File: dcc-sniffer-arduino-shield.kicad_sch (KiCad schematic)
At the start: 9 parts, among them J1 MV132, U1 6N137

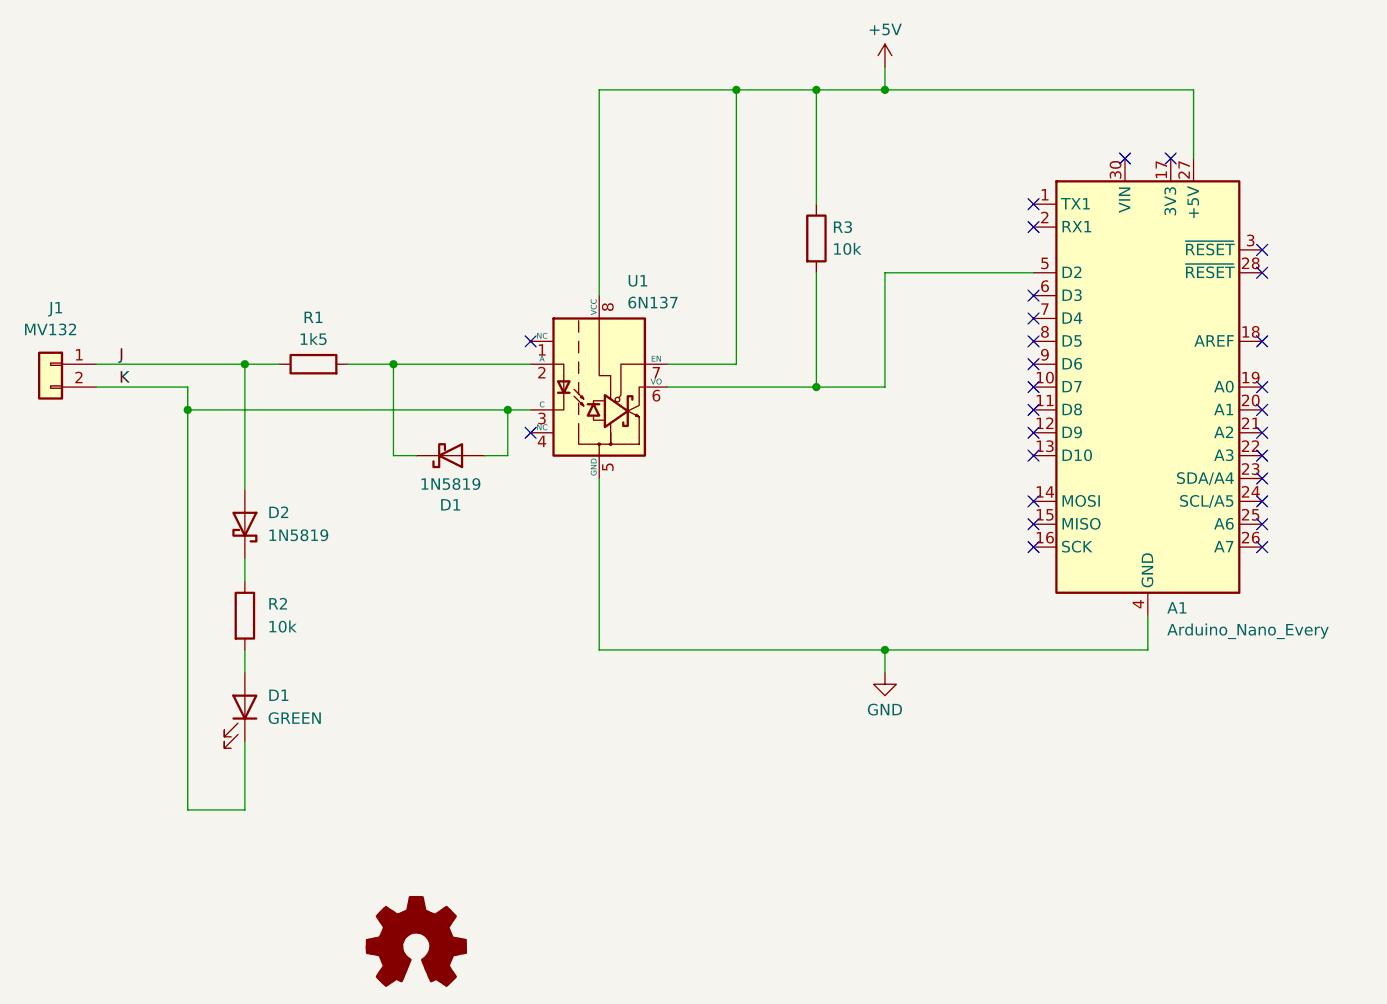
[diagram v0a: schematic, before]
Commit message: Route PCB.
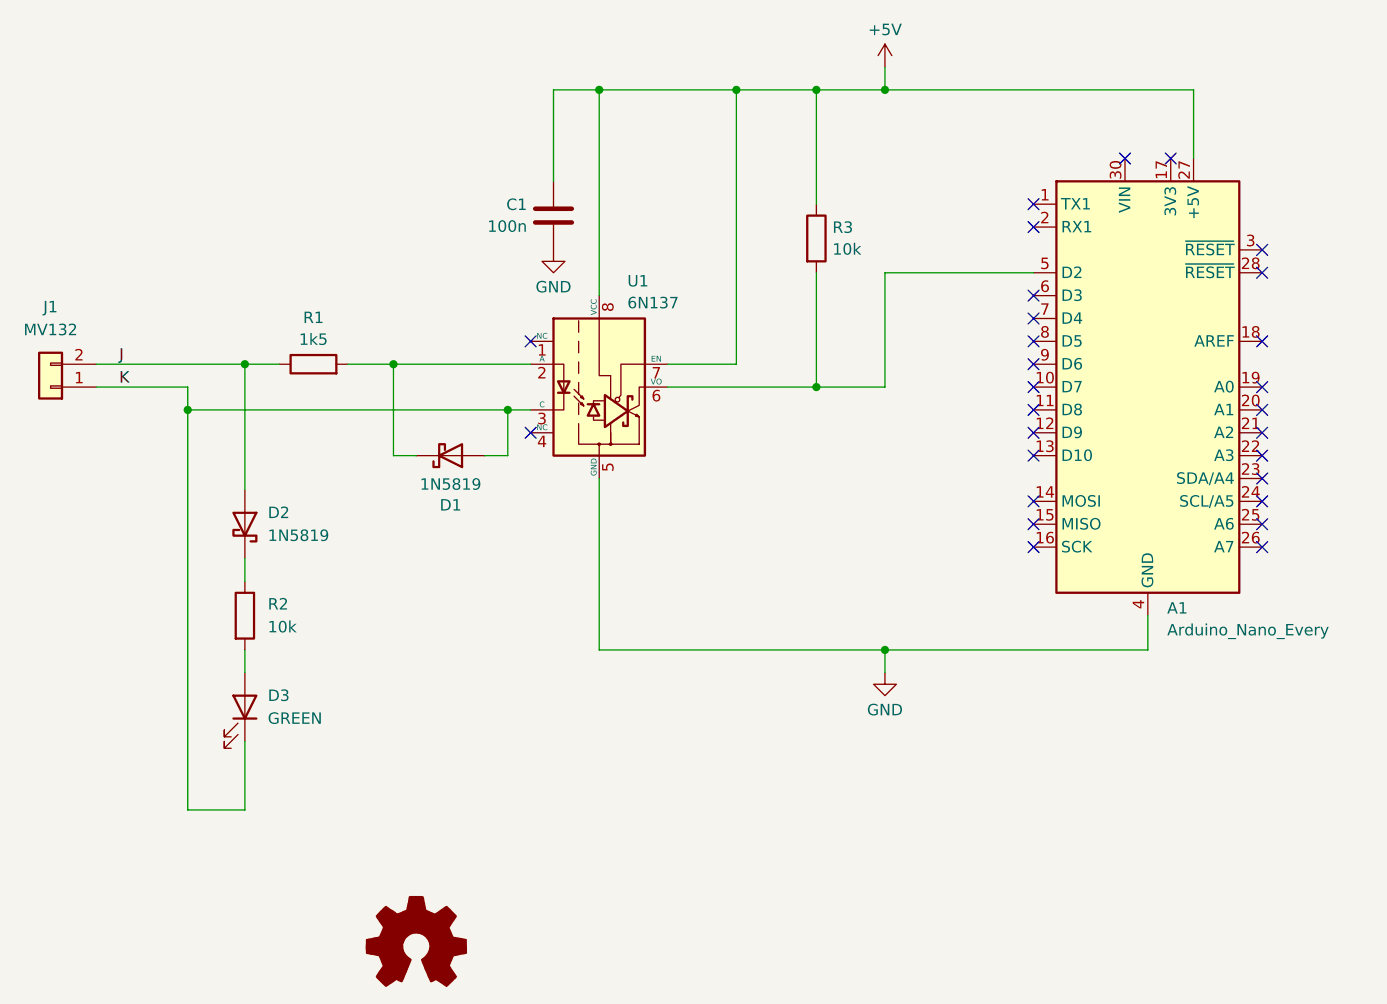
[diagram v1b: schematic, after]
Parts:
- added C1: 100n, Capacitor_SMD:C_0805_2012Metric_Pad1.18x1.45mm_HandSolder, symbol Device:C
- renumbered D1 to D3
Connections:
- net +5V: now also C1.1
- net GND: now also C1.2
- net J: now also J1.2 (Pin_2); no longer J1.1 (Pin_1)
- net K: now also J1.1 (Pin_1); no longer J1.2 (Pin_2)
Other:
- moved on the sheet: J1
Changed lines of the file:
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@@
+	)
+	(junction
+		(at 93.98 24.13)
+		(diameter 0)
+		(color 0 0 0 0)
 	)
 	(junction
@@
 	(wire
 		(pts
+			(xy 88.9 24.13) (xy 88.9 34.29)
+		)
+		(stroke
+			(width 0)
+			(type default)
+		)
+	)
+	(wire
+		(pts
 			(xy 48.26 104.14) (xy 48.26 59.69)
 		)
@@
 		(pts
 			(xy 54.61 54.61) (xy 54.61 68.58)
+		)
+		(stroke
+			(width 0)
+			(type default)
+		)
+	)
+	(wire
+		(pts
+			(xy 93.98 24.13) (xy 88.9 24.13)
 		)
 		(stroke
@@
 		(on_board yes)
 		(dnp no)
-		(property "Reference" "D1"
+		(property "Reference" "D3"
 			(at 57.15 91.44 90)
 			(effects
@@
 			(project ""
 				(path "/4adb1040-e115-4483-a004-02188402dddd"
-					(reference "D1")
+					(reference "D3")
 					(unit 1)
 				)
@@
 		(at 73.66 119.38 0)
 		(unit 1)
-		(exclude_from_sim no)
+		(exclude_from_sim yes)
 		(in_bom no)
 		(on_board no)
@@
 		)
 		(property "Description" "Open Hardware logo, small"
-			(at 73.66 119.38 0)
-			(effects
-				(font
-					(size 1.27 1.27)
-				)
-				(hide yes)
-			)
-		)
-		(property "Sim.Enable" "0"
 			(at 73.66 119.38 0)
 			(effects
@@
 	(symbol
 		(lib_id "power:GND")
+		(at 88.9 41.91 0)
+		(mirror y)
+		(unit 1)
+		(exclude_from_sim no)
+		(in_bom yes)
+		(on_board yes)
+		(dnp no)
+		(property "Reference" "#PWR03"
+			(at 88.9 48.26 0)
+			(effects
+				(font
+					(size 1.27 1.27)
+				)
+				(hide yes)
+			)
+		)
+		(property "Value" "GND"
+			(at 88.9 46.0431 0)
+			(effects
+				(font
+					(size 1.27 1.27)
+				)
+			)
+		)
+		(property "Footprint" ""
+			(at 88.9 41.91 0)
+			(effects
+				(font
+					(size 1.27 1.27)
+				)
+				(hide yes)
+			)
+		)
+		(property "Datasheet" ""
+			(at 88.9 41.91 0)
+			(effects
+				(font
+					(size 1.27 1.27)
+				)
+				(hide yes)
+			)
+		)
+		(property "Description" "Power symbol creates a global label with name \"GND\" , ground"
+			(at 88.9 41.91 0)
+			(effects
+				(font
+					(size 1.27 1.27)
+				)
+				(hide yes)
+			)
+		)
+		(pin "1"
+		)
+		(instances
+			(project "dcc-sniffer-arduino-shield"
+				(path "/4adb1040-e115-4483-a004-02188402dddd"
+					(reference "#PWR03")
+					(unit 1)
+				)
+			)
+		)
+	)
+	(symbol
+		(lib_id "power:GND")
 		(at 125.73 88.9 0)
 		(unit 1)
@@
 	(symbol
 		(lib_id "Connector_Generic:Conn_01x02")
-		(at 33.02 54.61 0)
+		(at 33.02 57.15 180)
+		(unit 1)
+		(exclude_from_sim no)
+		(in_bom yes)
+		(on_board yes)
+		(dnp no)
+		(property "Reference" "J1"
+			(at 33.02 48.26 0)
+			(effects
+				(font
+					(size 1.27 1.27)
+				)
+			)
+		)
+		(property "Value" "MV132"
+			(at 33.02 50.8 0)
+			(effects
+				(font
+					(size 1.27 1.27)
+				)
+			)
+		)
+		(property "Footprint" "TerminalBlock_4Ucon:TerminalBlock_4Ucon_1x02_P3.50mm_Horizontal"
+			(at 33.02 57.15 0)
+			(effects
+				(font
+					(size 1.27 1.27)
+				)
+				(hide yes)
+			)
+		)
+		(property "Datasheet" "~"
+			(at 33.02 57.15 0)
+			(effects
+				(font
+					(size 1.27 1.27)
+				)
+				(hide yes)
+			)
+		)
+		(property "Description" "Generic connector, single row, 01x02, script generated (kicad-library-utils/schlib/autogen/connector/)"
+			(at 33.02 57.15 0)
+			(effects
+				(font
+					(size 1.27 1.27)
+				)
+				(hide yes)
+			)
+		)
+		(pin "1"
+		)
+		(pin "2"
+		)
+		(instances
+			(project "dcc-sniffer-arduino-shield"
+				(path "/4adb1040-e115-4483-a004-02188402dddd"
+					(reference "J1")
+					(unit 1)
+				)
+			)
+		)
+	)
+	(symbol
+		(lib_id "Device:C")
+		(at 88.9 38.1 0)
 		(mirror y)
 		(unit 1)
@@
 		(on_board yes)
 		(dnp no)
-		(property "Reference" "J1"
-			(at 33.655 48.3757 0)
-			(effects
-				(font
-					(size 1.27 1.27)
-				)
-			)
-		)
-		(property "Value" "MV132"
-			(at 33.02 50.8 0)
-			(effects
-				(font
-					(size 1.27 1.27)
-				)
-			)
-		)
-		(property "Footprint" "TerminalBlock_4Ucon:TerminalBlock_4Ucon_1x02_P3.50mm_Horizontal"
-			(at 33.02 54.61 0)
+		(property "Reference" "C1"
+			(at 85.979 36.8878 0)
+			(effects
+				(font
+					(size 1.27 1.27)
+				)
+				(justify left)
+			)
+		)
+		(property "Value" "100n"
+			(at 85.979 39.3121 0)
+			(effects
+				(font
+					(size 1.27 1.27)
+				)
+				(justify left)
+			)
+		)
+		(property "Footprint" "Capacitor_SMD:C_0805_2012Metric_Pad1.18x1.45mm_HandSolder"
+			(at 87.9348 41.91 0)
 			(effects
 				(font
@@
 		)
 		(property "Datasheet" "~"
-			(at 33.02 54.61 0)
-			(effects
-				(font
-					(size 1.27 1.27)
-				)
-				(hide yes)
-			)
-		)
-		(property "Description" "Generic connector, single row, 01x02, script generated (kicad-library-utils/schlib/autogen/connector/)"
-			(at 33.02 54.61 0)
-			(effects
-				(font
-					(size 1.27 1.27)
-				)
-				(hide yes)
-			)
+			(at 88.9 38.1 0)
+			(effects
+				(font
+					(size 1.27 1.27)
+				)
+				(hide yes)
+			)
+		)
+		(property "Description" "Unpolarized capacitor"
+			(at 88.9 38.1 0)
+			(effects
+				(font
+					(size 1.27 1.27)
+				)
+				(hide yes)
+			)
+		)
+		(pin "2"
 		)
 		(pin "1"
 		)
-		(pin "2"
-		)
 		(instances
-			(project "dcc-sniffer-arduino-shield"
+			(project ""
 				(path "/4adb1040-e115-4483-a004-02188402dddd"
-					(reference "J1")
+					(reference "C1")
 					(unit 1)
 				)
